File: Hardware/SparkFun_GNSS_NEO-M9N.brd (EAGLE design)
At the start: 64.9 x 38 mm, 65 parts, among them J1 MICROMOD_STANDARD, U1 U-BLOX_NEO-M9N, U2 3.3V, U3 EEPROM, U4 74HC1G04

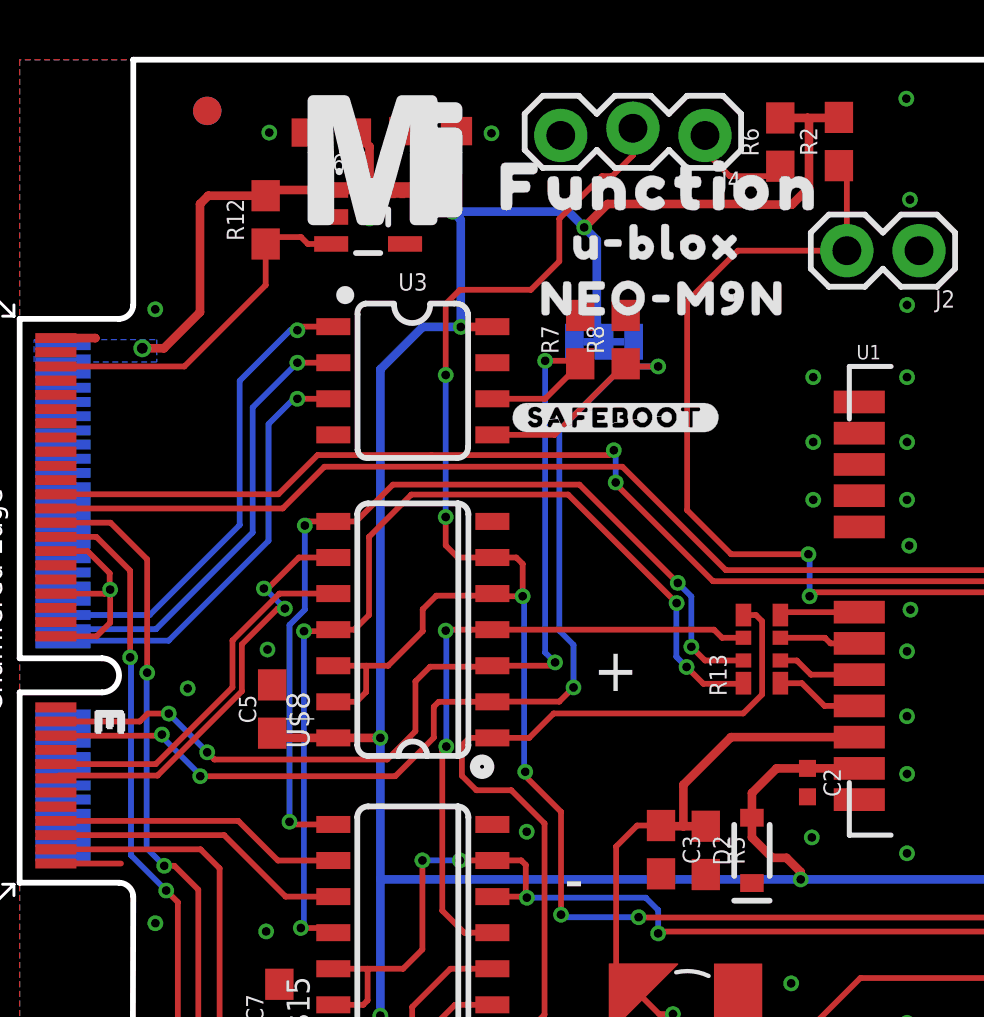
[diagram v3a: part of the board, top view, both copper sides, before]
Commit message: Fixes various traces
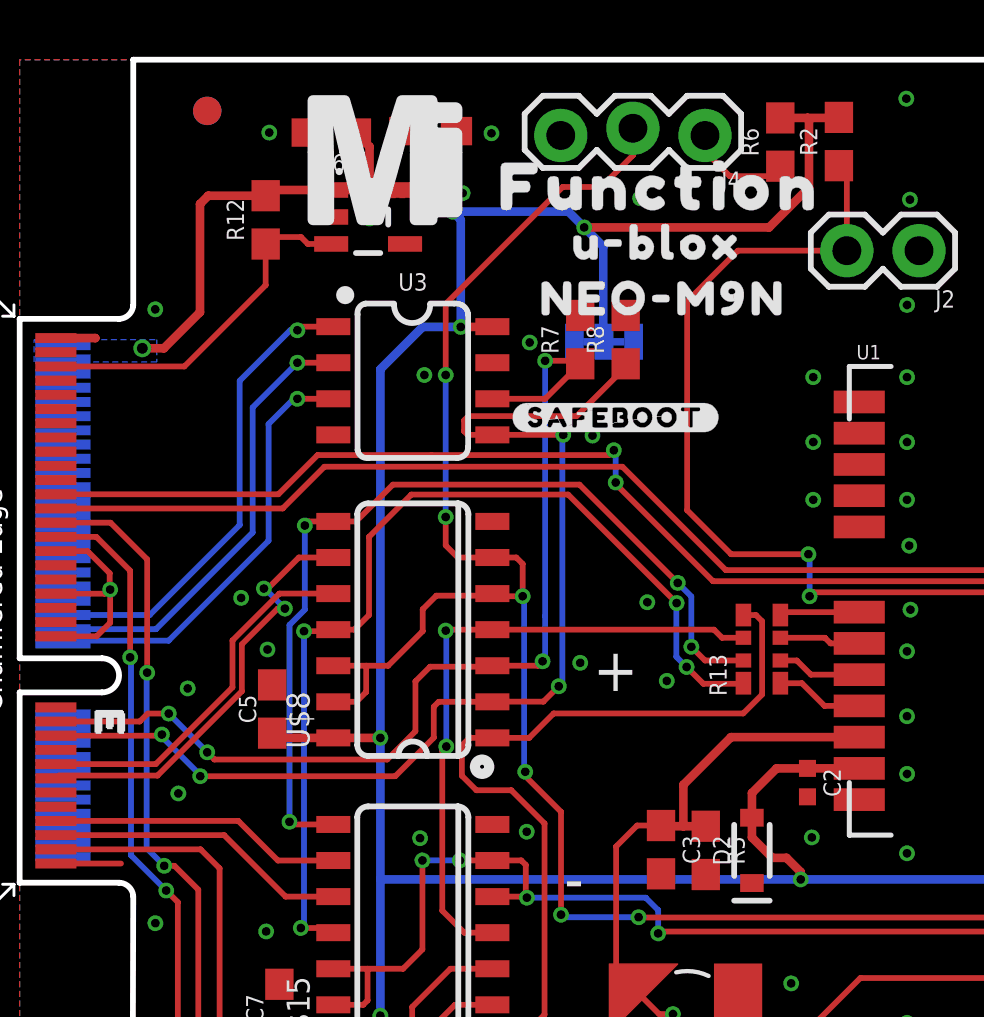
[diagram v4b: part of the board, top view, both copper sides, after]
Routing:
- net SDA: track 41.4 -> 39.9 mm
- net D_SEL: track 74.9 -> 74.0 mm
- net SCL: track 36.4 -> 35.9 mm
- net GND: vias 145 -> 156
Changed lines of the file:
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@@
 <setting verticaltext="up"/>
 </settings>
-<grid distance="0.5" unitdist="mm" unit="mm" style="dots" multiple="1" display="yes" altdistance="0.01" altunitdist="mm" altunit="mm"/>
+<grid distance="0.01" unitdist="inch" unit="inch" style="dots" multiple="1" display="yes" altdistance="0.001" altunitdist="inch" altunit="inch"/>
 <layers>
 <layer number="1" name="Top" color="4" fill="1" visible="yes" active="yes"/>
@@
 <wire x1="16.633" y1="28.692" x2="15.53" y2="28.692" width="0.3048" layer="1"/>
 <via x="15.53" y="28.692" extent="1-16" drill="0.3048"/>
-<wire x1="20.574" y1="28.1686" x2="20.32" y2="28.4226" width="0.3048" layer="16"/>
-<wire x1="20.32" y1="28.4226" x2="20.32" y2="31.75" width="0.3048" layer="16"/>
-<wire x1="20.32" y1="31.75" x2="19.8755" y2="32.1945" width="0.3048" layer="16"/>
+<wire x1="20.574" y1="28.1686" x2="20.5486" y2="28.194" width="0.3048" layer="16"/>
+<wire x1="20.5486" y1="28.194" x2="20.5486" y2="31.5214" width="0.3048" layer="16"/>
+<wire x1="20.5486" y1="31.5214" x2="19.8755" y2="32.1945" width="0.3048" layer="16"/>
 <wire x1="19.8755" y1="32.1945" x2="19.3192" y2="32.7508" width="0.3048" layer="16"/>
 <wire x1="19.3192" y1="32.7508" x2="15.24" y2="32.7508" width="0.3048" layer="16"/>
-<wire x1="19.8755" y1="32.1945" x2="20.701" y2="33.02" width="0.3048" layer="1"/>
+<wire x1="27.79" y1="33.6" x2="26.3845" y2="32.1945" width="0.3048" layer="1"/>
+<wire x1="19.8755" y1="32.1945" x2="26.3845" y2="32.1945" width="0.3048" layer="1"/>
 <via x="19.8755" y="32.1945" extent="1-16" drill="0.3048"/>
 <wire x1="44.704" y1="9.6266" x2="43.9674" y2="8.89" width="0.3048" layer="16"/>
@@
 <via x="27.5" y="9.24" extent="1-16" drill="0.3048"/>
 <wire x1="25.781" y1="10.719" x2="26.5" y2="10" width="0.3048" layer="1"/>
-<wire x1="20.701" y1="33.02" x2="25.98" y2="33.02" width="0.3048" layer="1"/>
-<wire x1="25.98" y1="33.02" x2="26" y2="33" width="0.3048" layer="1"/>
-<wire x1="26" y1="33" x2="27.19" y2="33" width="0.3048" layer="1"/>
-<wire x1="27.19" y1="33" x2="27.79" y2="33.6" width="0.3048" layer="1"/>
 <wire x1="28.844" y1="36.069" x2="28.825" y2="36.05" width="0.3048" layer="1"/>
 <wire x1="28.825" y1="36.05" x2="27.74" y2="36.05" width="0.3048" layer="1"/>
@@
 <wire x1="44.704" y1="17.916" x2="44.704" y2="18.3134" width="0.2032" layer="1"/>
 <wire x1="47.5" y1="19.5" x2="45.73" y2="17.73" width="0.2032" layer="1"/>
-<wire x1="13.5683" y1="33.5128" x2="13.6788" y2="35.5854" width="0" layer="19" extent="1-1"/>
 </signal>
 <signal name="GND">
@@
 <via x="27.162" y="5.581" extent="1-16" drill="0.3048"/>
 <via x="26.942" y="2.551" extent="1-16" drill="0.3048"/>
+<via x="17.9578" y="28.1432" extent="1-16" drill="0.3048"/>
+<via x="14.2494" y="27.0002" extent="1-16" drill="0.3048"/>
+<via x="20.1676" y="24.8666" extent="1-16" drill="0.3048"/>
+<via x="19.7358" y="16.8656" extent="1-16" drill="0.3048"/>
+<via x="22.098" y="18.9992" extent="1-16" drill="0.3048"/>
+<via x="22.7838" y="16.2306" extent="1-16" drill="0.3048"/>
+<via x="7.7978" y="19.1516" extent="1-16" drill="0.3048"/>
+<via x="5.588" y="12.2682" extent="1-16" drill="0.3048"/>
+<via x="14.097" y="10.6934" extent="1-16" drill="0.3048"/>
+<via x="21.844" y="33.2232" extent="1-16" drill="0.3048"/>
+<via x="15.5956" y="33.401" extent="1-16" drill="0.3048"/>
 <wire x1="60.706" y1="14.732" x2="63.9826" y2="14.732" width="0" layer="19" extent="1-1"/>
 <wire x1="59.0648" y1="13.385" x2="60.706" y2="14.732" width="0" layer="19" extent="1-1"/>
 <wire x1="61.6966" y1="7.112" x2="59.0648" y2="6.935" width="0" layer="19" extent="1-1"/>
 <wire x1="64.262" y1="7.2136" x2="61.6966" y2="7.112" width="0" layer="19" extent="1-1"/>
-<wire x1="16.643" y1="21.844" x2="16.643" y2="27.432" width="0" layer="19" extent="1-1"/>
 </signal>
 <signal name="SCL/SCK">
@@
 <wire x1="15" y1="22" x2="15" y2="27" width="0.2032" layer="16"/>
 <wire x1="15" y1="27" x2="15" y2="29.5" width="0.2032" layer="1"/>
-<wire x1="15.5" y1="30" x2="15" y2="29.5" width="0.2032" layer="1"/>
-<wire x1="15.5" y1="30" x2="18" y2="30" width="0.2032" layer="1"/>
-<wire x1="18" y1="30" x2="19" y2="31" width="0.2032" layer="1"/>
-<wire x1="19" y1="31" x2="19" y2="32.5" width="0.2032" layer="1"/>
-<wire x1="19" y1="32.5" x2="20.5" y2="34" width="0.2032" layer="1"/>
-<wire x1="20.5" y1="34" x2="20.86" y2="34" width="0.2032" layer="1"/>
-<wire x1="20.86" y1="34" x2="21.59" y2="34.73" width="0.2032" layer="1"/>
+<wire x1="15" y1="29.5" x2="19.119" y2="33.619" width="0.2032" layer="1"/>
+<wire x1="19.119" y1="33.619" x2="20.479" y2="33.619" width="0.2032" layer="1"/>
+<wire x1="20.479" y1="33.619" x2="21.59" y2="34.73" width="0.2032" layer="1"/>
 <wire x1="21.59" y1="34.73" x2="21.59" y2="35.687" width="0.2032" layer="1"/>
 </signal>
@@
 <wire x1="6.359" y1="12.874" x2="13.224" y2="12.874" width="0.2032" layer="1"/>
 <wire x1="13.224" y1="12.874" x2="14.58" y2="14.23" width="0.2032" layer="1"/>
-<wire x1="16.643" y1="24.892" x2="18.8332" y2="24.892" width="0.2032" layer="1"/>
+<wire x1="16.643" y1="24.892" x2="19.138" y2="24.892" width="0.2032" layer="1"/>
 <wire x1="14.58" y1="14.23" x2="14.58" y2="15.32" width="0.2032" layer="1"/>
 <wire x1="14.58" y1="15.32" x2="14.754" y2="15.494" width="0.2032" layer="1"/>
 <wire x1="14.754" y1="15.494" x2="16.643" y2="15.494" width="0.2032" layer="1"/>
 <wire x1="16.643" y1="15.494" x2="16.649" y2="15.5" width="0.2032" layer="1"/>
-<wire x1="16.649" y1="15.5" x2="19" y2="15.5" width="0.2032" layer="1"/>
-<wire x1="19" y1="15.5" x2="19.5" y2="16" width="0.2032" layer="1"/>
-<via x="19.5" y="16" extent="1-16" drill="0.3048"/>
-<wire x1="19.5" y1="16" x2="19.5" y2="17.5" width="0.2032" layer="16"/>
-<wire x1="19.5" y1="17.5" x2="19" y2="18" width="0.2032" layer="16"/>
-<wire x1="19" y1="18" x2="19" y2="25.0588" width="0.2032" layer="16"/>
-<wire x1="19" y1="25.0588" x2="21.2412" y2="27.3" width="0.2032" layer="16"/>
-<wire x1="21.2412" y1="27.3" x2="22.48" y2="27.3" width="0.2032" layer="16"/>
-<via x="22.48" y="27.3" extent="1-16" drill="0.3048"/>
-<wire x1="22.48" y1="27.3" x2="21.4308" y2="27.3" width="0.2032" layer="1"/>
-<wire x1="21.4308" y1="27.3" x2="21.336" y2="27.3948" width="0.2032" layer="1"/>
-<wire x1="18.8332" y1="24.892" x2="21.336" y2="27.3948" width="0.2032" layer="1"/>
+<wire x1="16.649" y1="15.5" x2="18.44" y2="15.5" width="0.2032" layer="1"/>
+<wire x1="18.44" y1="15.5" x2="18.98" y2="16.04" width="0.2032" layer="1"/>
+<via x="18.98" y="16.04" extent="1-16" drill="0.3048"/>
+<wire x1="21.4308" y1="27.3" x2="21.3936" y2="27.3372" width="0.2032" layer="1"/>
+<wire x1="21.3936" y1="27.3372" x2="21.336" y2="27.3948" width="0.2032" layer="1"/>
+<wire x1="18.98" y1="16.04" x2="19.107" y2="16.167" width="0.2032" layer="16"/>
+<wire x1="19.107" y1="24.861" x2="19.107" y2="16.167" width="0.2032" layer="16"/>
+<wire x1="19.107" y1="24.861" x2="19.138" y2="24.892" width="0.2032" layer="16"/>
+<via x="19.138" y="24.892" extent="1-16" drill="0.3048"/>
+<wire x1="16.643" y1="24.892" x2="15.7734" y2="24.892" width="0.2032" layer="1"/>
+<wire x1="15.7734" y1="24.892" x2="15.6464" y2="25.019" width="0.2032" layer="1"/>
+<wire x1="15.6464" y1="25.019" x2="15.6464" y2="25.4" width="0.2032" layer="1"/>
+<wire x1="15.6464" y1="25.4" x2="15.7988" y2="25.5524" width="0.2032" layer="1"/>
+<wire x1="19.6088" y1="25.5524" x2="21.3936" y2="27.3372" width="0.2032" layer="1"/>
+<wire x1="15.7988" y1="25.5524" x2="19.6088" y2="25.5524" width="0.2032" layer="1"/>
 </signal>
 <signal name="SCK">
@@
 <wire x1="18.503" y1="26.162" x2="19.6705" y2="27.3295" width="0.2032" layer="1"/>
 <wire x1="19.6705" y1="27.3295" x2="19.7358" y2="27.3948" width="0.2032" layer="1"/>
-<wire x1="16.643" y1="16.764" x2="18.734" y2="16.764" width="0.2032" layer="1"/>
-<wire x1="18.734" y1="16.764" x2="18.85" y2="16.88" width="0.2032" layer="1"/>
-<via x="18.85" y="16.88" extent="1-16" drill="0.3048"/>
-<wire x1="18.85" y1="16.88" x2="18.5" y2="17.23" width="0.2032" layer="16"/>
-<wire x1="18.5" y1="17.23" x2="18.5" y2="27.5" width="0.2032" layer="16"/>
+<wire x1="16.643" y1="16.764" x2="18.254" y2="16.764" width="0.2032" layer="1"/>
+<wire x1="18.254" y1="16.764" x2="18.41" y2="16.92" width="0.2032" layer="1"/>
+<via x="18.41" y="16.92" extent="1-16" drill="0.3048"/>
+<wire x1="18.41" y1="16.92" x2="18.5" y2="17.01" width="0.2032" layer="16"/>
+<wire x1="18.5" y1="17.01" x2="18.5" y2="18.5" width="0.2032" layer="16"/>
 <via x="18.5" y="27.5" extent="1-16" drill="0.3048"/>
+<wire x1="18.5" y1="18.5" x2="18.5" y2="27.5" width="0.2032" layer="16"/>
 <wire x1="18.5" y1="27.5" x2="19.5" y2="27.5" width="0.2032" layer="1"/>
 <wire x1="19.5" y1="27.5" x2="19.6705" y2="27.3295" width="0.2032" layer="1"/>

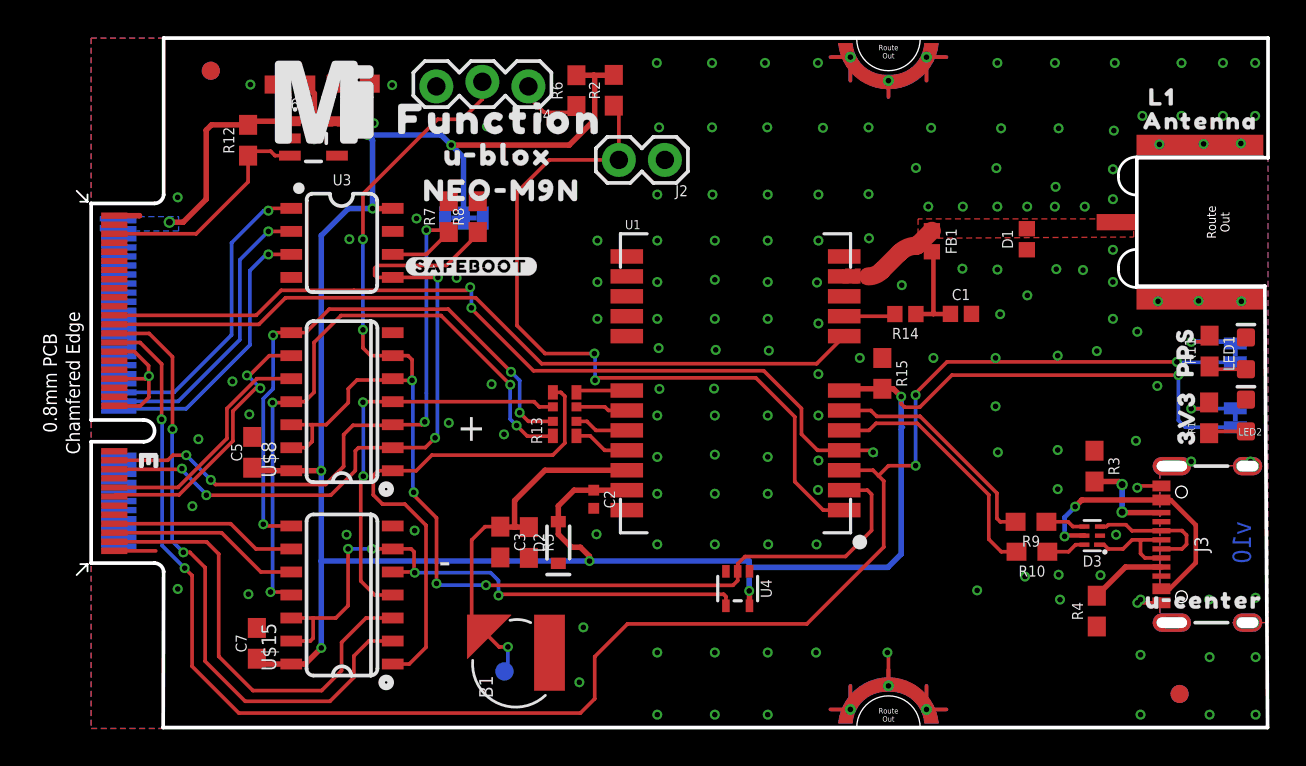
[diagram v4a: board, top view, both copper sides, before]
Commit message: Moves silk around, seeds new vias around the PCB
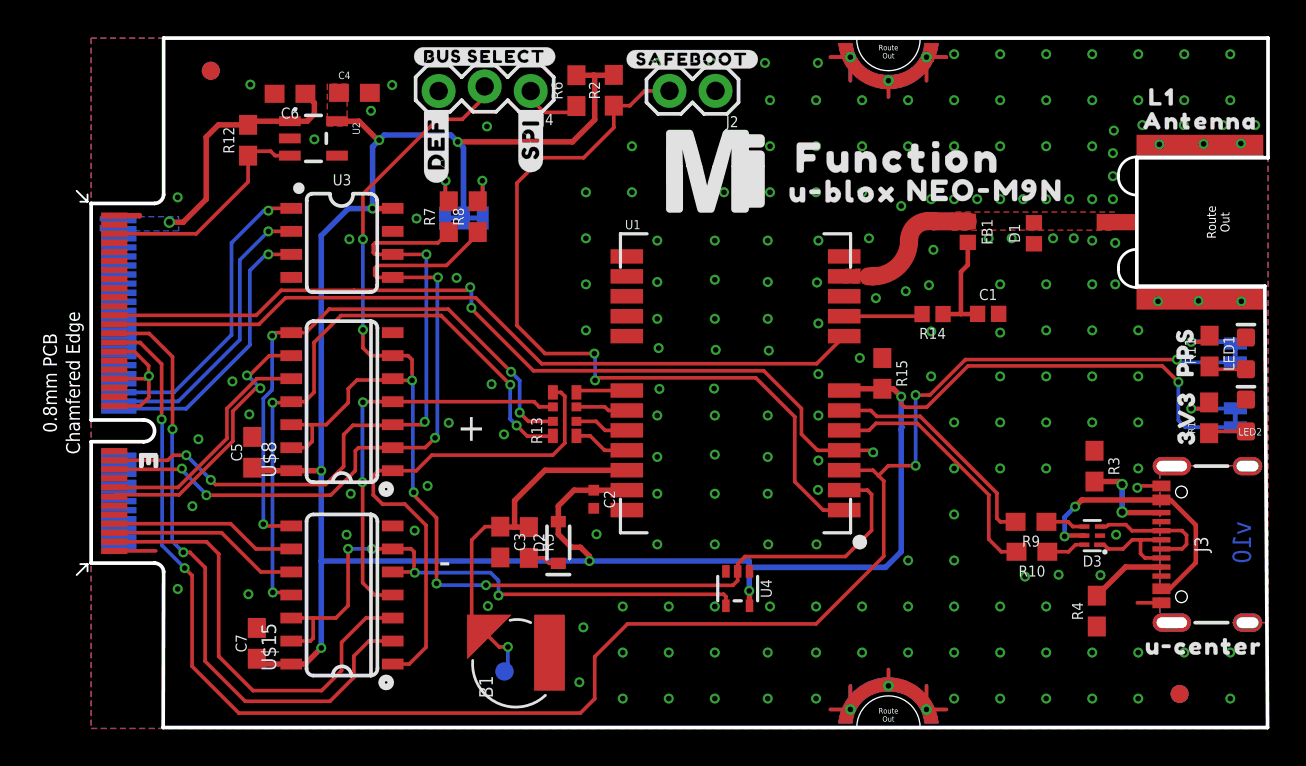
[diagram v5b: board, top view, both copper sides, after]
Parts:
- added U$16: (no value), top:#DEF#521
- added U$17: (no value), top:#SPI#520
- added U$18: (no value), top:#BUS_SELECT#509
- moved U$6 26.7 mm to (49.3, 29.7)
- moved U$3 22.1 mm to (44.5, 31.5)
- moved U$11 21.9 mm to (34.5, 30.8)
- moved U$5 19.2 mm to (41.5, 29.6)
- moved U$4 16.7 mm to (33.2, 36.9)
- moved J2 4.72 mm to (34.5, 35.2)
- moved U$9 2.54 mm to (61.4, 4.54)
- moved FB1 2.05 mm to (48.4, 27.4)
- moved C1 1.50 mm to (49.5, 22.9)
- moved R14 1.50 mm to (46.4, 22.9)
- moved D1 0.51 mm to (52.0, 27.3)
- moved C4 0.51 mm to (14.5, 35.1)
- moved C6 0.51 mm to (11.0, 35.0)
- moved J4 0.28 mm to (24.3, 35.3)
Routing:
- net N$5: track 0.00 -> 3.30 mm, vias 0 -> 1
- net N$8: track 0.00 -> 3.27 mm, vias 0 -> 1
- net GPS_ANT1: track 4.41 -> 6.76 mm
- net !SAFE: track 42.2 -> 44.4 mm
- net SCL: track 35.9 -> 37.9 mm
- net N$6: track 0.00 -> 1.75 mm
- net VCC_RF: track 2.84 -> 4.34 mm
- net N$3: track 5.38 -> 6.17 mm
- net GND: track 18.9 -> 19.7 mm, vias 156 -> 205
- net VCC: track 14.5 -> 13.8 mm
